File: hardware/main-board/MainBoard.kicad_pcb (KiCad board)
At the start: 4 copper layers, 145 parts, among them J1 Conn_01x03_Pin, J10 USB_C_Receptacle_USB2.0_14P, J11 Conn_02x05_Odd_Even, J12 Conn_01x02_Pin, J13 Conn_01x02_Pin, J2 Conn_01x03_Pin, J3 Conn_01x03_Pin, J4 Conn_01x03_Pin, J5 Conn_01x02_Pin, J6 Conn_01x02_Pin, J7 Conn_01x02_Pin, J8 Conn_01x02_Pin, J9 Barrel_Jack, SW1 SW_SP3T, SW2 SW_SP3T, SW3 SW_SPST, SW4 SW_SPST, U1 CD22M3494MQZ, U10 TL071, U11 CD22M3494MQZ, U12 CD22M3494MQZ, U13 TL071, U14 AD5263BRUZ200, U15 AD5263BRUZ200, U16 TL071, U17 CD22M3494MQZ, U18 CD22M3494MQZ, U19 TL071, U2 TL081, U20 AD5263BRUZ200, U21 AD5263BRUZ200, U22 TL071, U23 CD22M3494MQZ, U24 CD22M3494MQZ, U25 TL071, U26 AD5263BRUZ200, U27 AD5263BRUZ200, U28 TL071, U29 CD22M3494MQZ, U3 TL071, U30 CD22M3494MQZ, U31 XTPS55285VALR, U32 TPS54202DDC, U33 LM2776, U34 74HC164, U35 FT232RL, U36 74HC164, U37 STM32F091RCTx, U38 74HC164, U4 TL071, U5 TL071, U6 TL071, U7 TL071, U8 AD5263BRUZ200, U9 AD5263BRUZ200

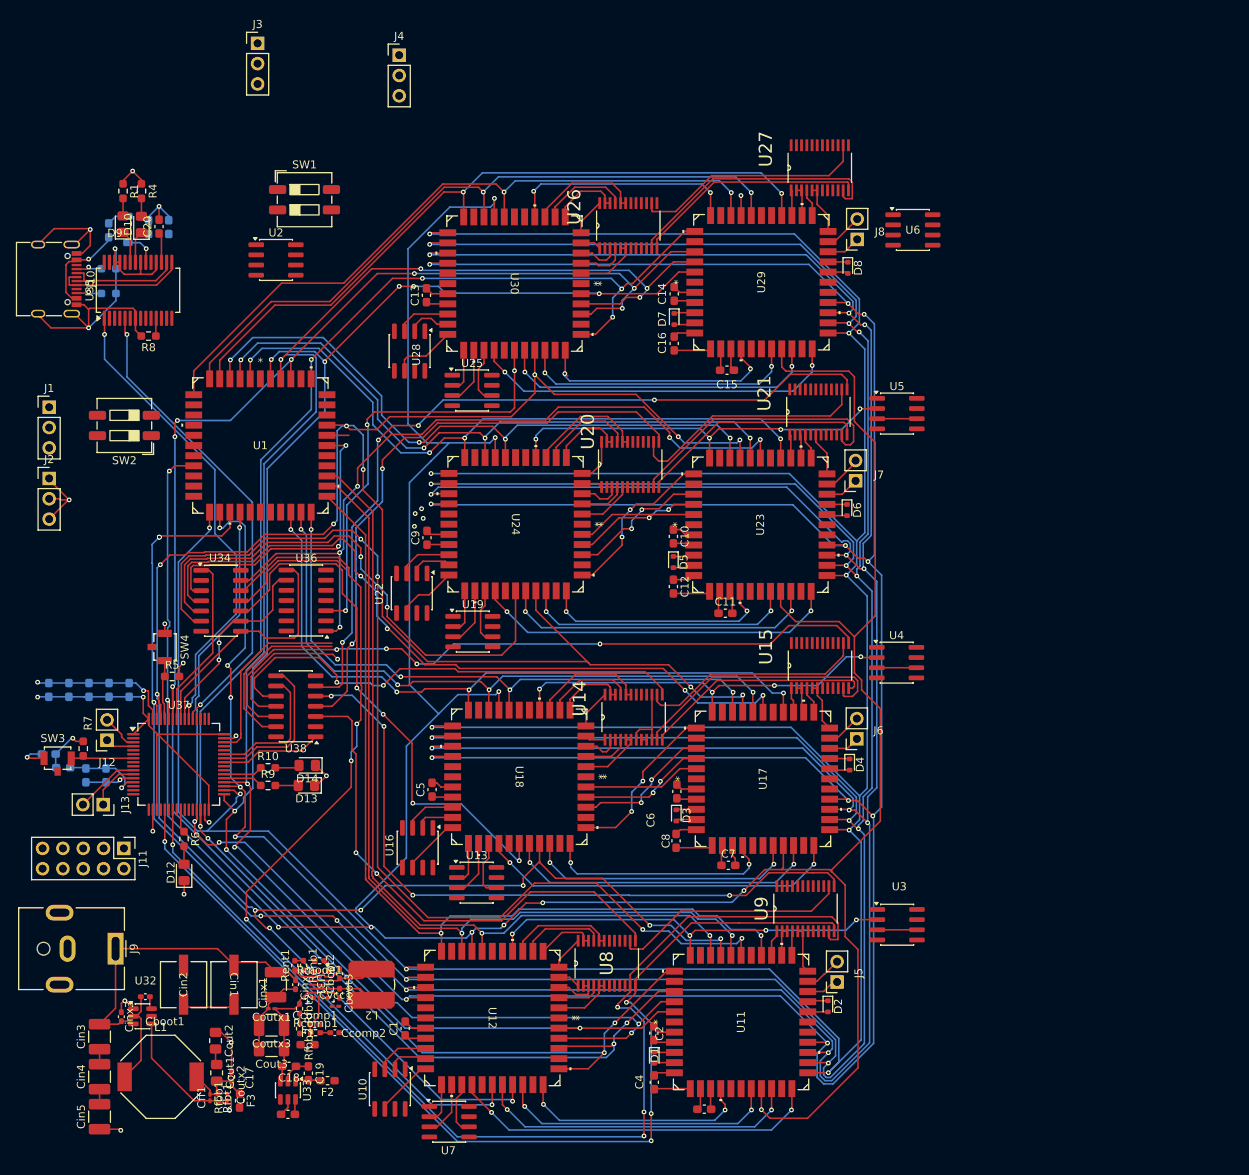
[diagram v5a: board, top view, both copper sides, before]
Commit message: completed AX and AY on all cells, started ground and power plane
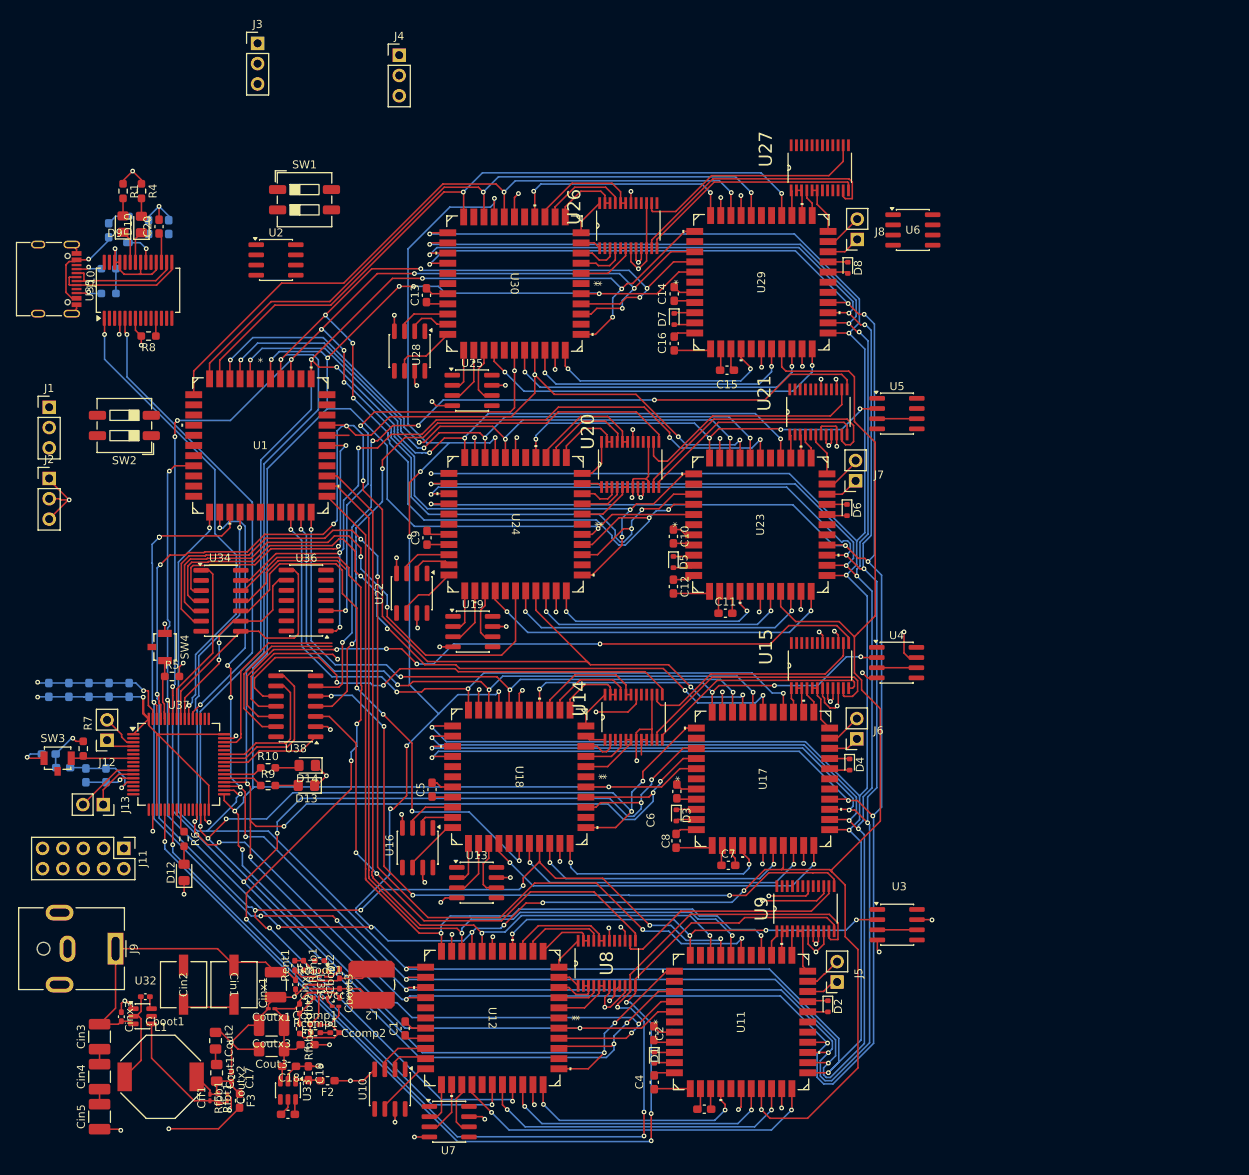
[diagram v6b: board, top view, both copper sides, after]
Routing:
- net /MicroController/MT_RST: track 261.6 -> 376.9 mm, vias 14 -> 18
- net /MicroController/MT_AX3: track 252.5 -> 367.7 mm, vias 13 -> 16
- net /MicroController/MT_AY2: track 256.4 -> 366.6 mm, vias 13 -> 14
- net +5V: track 8.65 -> 113.4 mm, vias 0 -> 30
- net /MicroController/MT_AX0: track 231.3 -> 319.2 mm, vias 9 -> 10
- net -5V: track 0.00 -> 60.0 mm, vias 0 -> 24
- net GNDPWR: track 28.6 -> 50.8 mm, vias 4 -> 7
- net +3.3V: track 62.8 -> 74.8 mm, vias 5 -> 7
- net GND: track 118.9 -> 124.9 mm, vias 15 -> 28
- net Net-(U31-FB_INT_N): track 1.30 -> 3.95 mm
- net /Power Supply/5V: track 15.9 -> 18.2 mm
- net /MicroController/MT_AY1: track 434.4 -> 436.5 mm
- net Net-(U31-EN_UVLO): track 1.10 -> 3.02 mm
- net /MicroController/MT_AX2: track 441.4 -> 439.6 mm
- net Net-(U31-MODE): track 0.00 -> 1.57 mm
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- added copper zone on In1.Cu, net +3.3V
- added copper zone on In2.Cu, net GND
- added copper zone on In2.Cu, net GNDPWR

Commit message: Almost done with the control
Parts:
- moved U2 11.1 mm to (84.5, 44.0)
- moved SW1 8.72 mm to (88.9, 38.9)
- moved U6 7.93 mm to (169.1, 41.1)
- moved SW2 4.29 mm to (71.4, 77.3)
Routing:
- net /MicroController/BRUZ_NCS_7: track 21.7 -> 150.6 mm, vias 0 -> 2
- net /MicroController/MT_CS_5: track 16.4 -> 121.0 mm, vias 0 -> 4
- net /MicroController/BRUZ_NCS_5: track 18.6 -> 119.0 mm, vias 1 -> 2
- net /MicroController/MT_DAT: track 361.5 -> 432.8 mm
- net /MicroController/SWDIO: track 23.5 -> 0.00 mm
- net /Cell_3_Out: track 29.1 -> 51.7 mm, vias 2 -> 4
- net /Cell_3_Buff: track 0.00 -> 4.95 mm
- net /MicroController/MT_RST: track 376.9 -> 381.7 mm
- net /MicroController/MT_AY2: track 366.6 -> 368.6 mm
- net /MicroController/SPI1_MOSI: track 236.7 -> 238.1 mm
- net /MicroController/MT_STB: track 417.2 -> 418.6 mm
- net /MicroController/SPI1_SCK: track 218.8 -> 220.0 mm
- net /STD3/Y1: track 86.6 -> 87.4 mm
- net /MicroController/MT_CS_1: track 93.3 -> 94.0 mm
- net /STD3/Y2: track 87.4 -> 87.9 mm
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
